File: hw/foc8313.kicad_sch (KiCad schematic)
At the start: 66 parts, among them J1 Tag Connect, J2 CAN, J3 CAN, J4 Aux, P1 USB_C_Plug, SW1 SW_SPST, U1 DRV8313PWP, U10 XC6206P332MR, U2 STM32F103CBTx, U4 AS5047D, U7 LMR36015SFBRNXR, U9 ZD24C08AE1-STGMT, X1 X322516MLB4SI

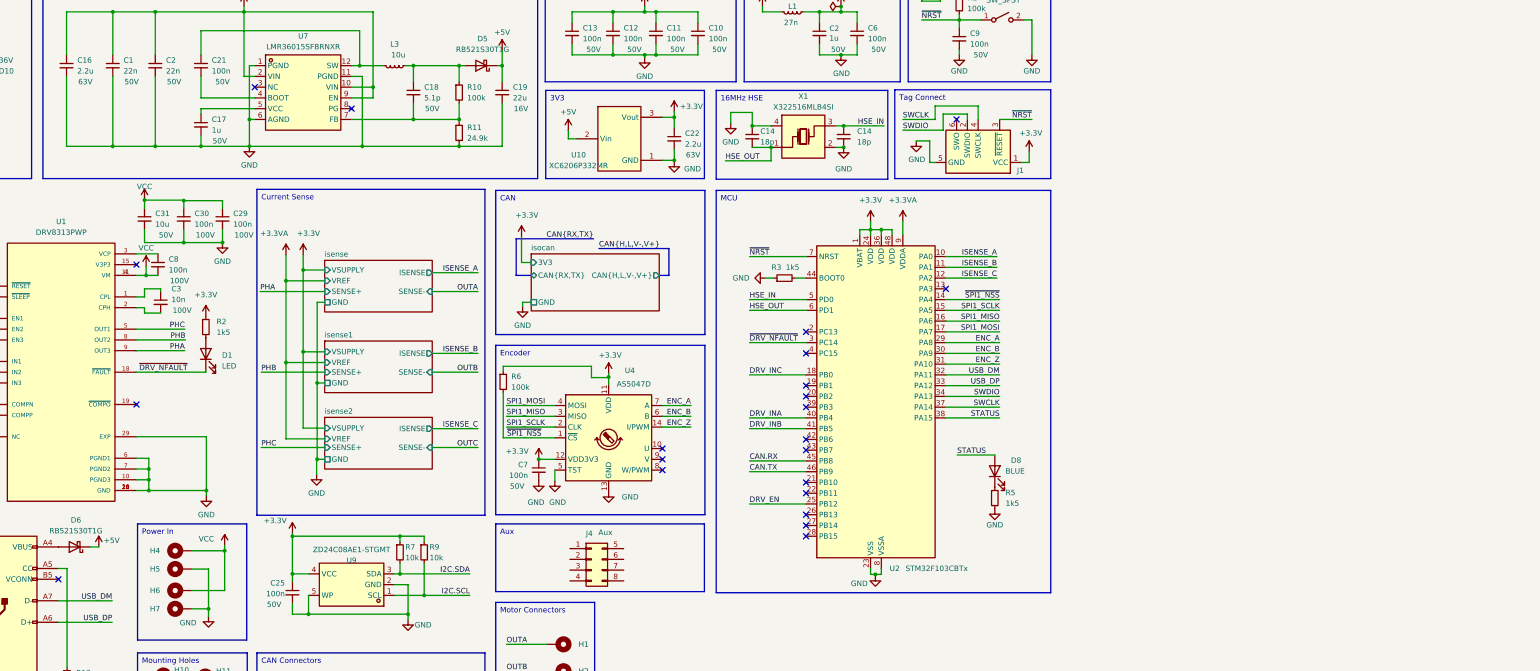
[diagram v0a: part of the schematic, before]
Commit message: [Hw] Cleaning up 5V section
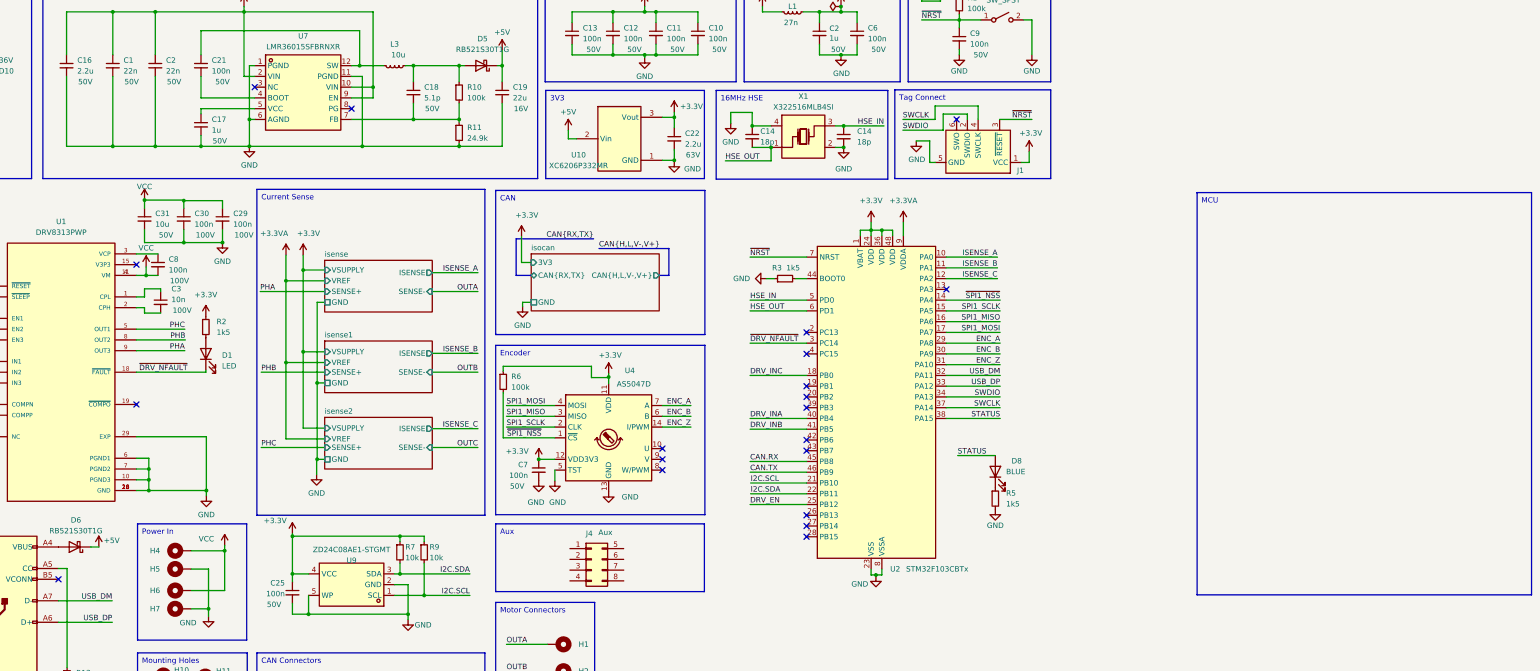
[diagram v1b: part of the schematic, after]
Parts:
- C16: LCSC C6119940 -> C377773; Rating 63V -> 50V
- C18: footprint Capacitor_SMD:C_0603_1608Metric -> Capacitor_SMD:C_0402_1005Metric; LCSC C519110 -> C710655
- C22: LCSC C6119940 -> C377773
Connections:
- net I2C.SCL: now also U2.21 (PB10)
- net I2C.SDA: now also U2.22 (PB11)
- no-connect marks 24 -> 22

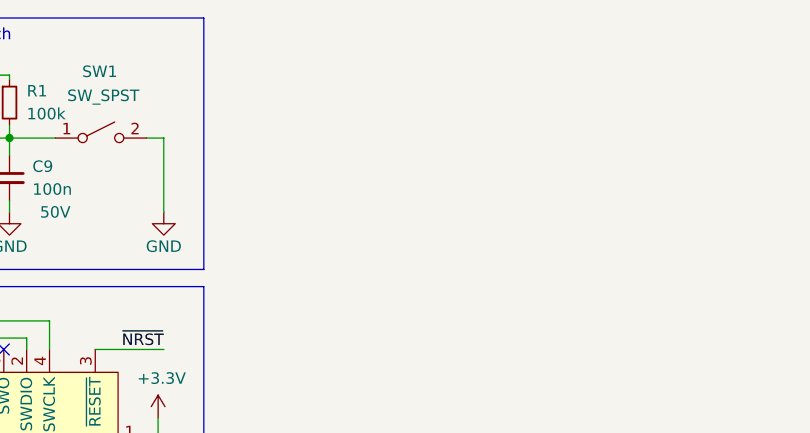
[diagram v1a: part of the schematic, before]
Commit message: [Hw] User button, tag connect placement, eeprom placement
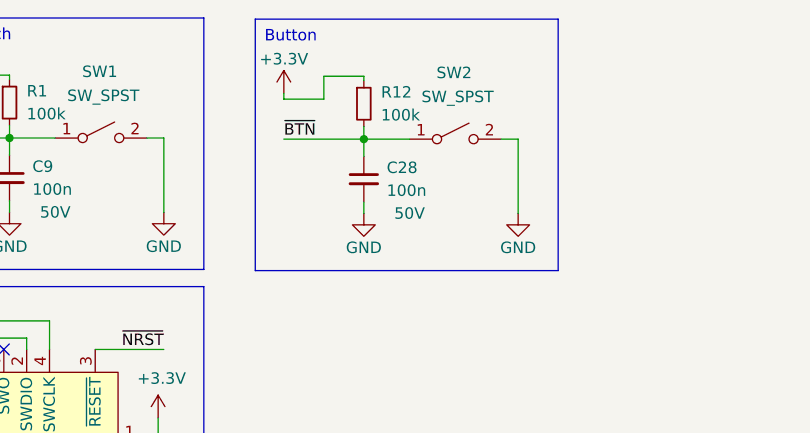
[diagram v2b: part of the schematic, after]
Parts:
- added C28: 100n, Capacitor_SMD:C_0402_1005Metric, symbol Device:C_Small
- added R12: 100k, Resistor_SMD:R_0402_1005Metric, symbol Device:R_Small
- added SW2: SW_SPST, easyeda:SW-SMD_L4.7-W3.5-P3.35-EH, symbol Switch:SW_SPST
- J2, J3: footprint Connector_JST:JST_GH_SM04B-GHS-TB_1x04-1MP_P1.25mm_Horizontal -> easyeda:CONN-SMD_4P-P1.00_INCP_IPCW100W14XXXXR
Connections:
- net +3.3V: now also R12.1
- net GND: now also C28.2, SW2.2 (B)
- new net ~{BTN}: C28.1, R12.2, SW2.1 (A)
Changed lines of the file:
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@@
   (junction (at 86.36 81.153) (diameter 0) (color 0 0 0 0)
   )
+  (junction (at 299.72 28.702) (diameter 0) (color 0 0 0 0)
+  )
   (junction (at 242.062 78.232) (diameter 0) (color 0 0 0 0)
   )
@@
     (stroke (width 0) (type default))
   )
+  (wire (pts (xy 299.72 36.957) (xy 299.72 35.687))
+    (stroke (width 0) (type default))
+  )
   (wire (pts (xy 239.522 78.232) (xy 242.062 78.232))
     (stroke (width 0) (type default))
@@
     (stroke (width 0) (type default))
   )
+  (wire (pts (xy 290.83 24.257) (xy 290.83 23.622))
+    (stroke (width 0) (type default))
+  )
   (wire (pts (xy 153.416 182.372) (xy 163.068 182.372))
     (stroke (width 0) (type default))
@@
     (stroke (width 0) (type default))
   )
+  (wire (pts (xy 290.83 28.702) (xy 299.72 28.702))
+    (stroke (width 0) (type default))
+  )
   (wire (pts (xy 19.05 93.98) (xy 30.48 93.98))
     (stroke (width 0) (type default))
@@
     (stroke (width 0) (type default))
   )
+  (wire (pts (xy 299.72 27.305) (xy 299.72 28.702))
+    (stroke (width 0) (type default))
+  )
   (wire (pts (xy 186.055 26.67) (xy 188.722 26.67))
     (stroke (width 0) (type default))
@@
     (stroke (width 0) (type default))
   )
+  (wire (pts (xy 316.865 36.957) (xy 316.865 28.702))
+    (stroke (width 0) (type default))
+  )
   (wire (pts (xy 78.994 163.322) (xy 86.868 163.322))
     (stroke (width 0) (type default))
@@
     (stroke (width 0) (type default))
   )
+  (wire (pts (xy 299.72 28.702) (xy 304.8 28.702))
+    (stroke (width 0) (type default))
+  )
   (wire (pts (xy 135.89 92.71) (xy 146.685 92.71))
     (stroke (width 0) (type default))
@@
     (stroke (width 0) (type default))
   )
+  (wire (pts (xy 290.83 24.257) (xy 295.275 24.257))
+    (stroke (width 0) (type default))
+  )
   (wire (pts (xy 135.89 107.315) (xy 146.685 107.315))
     (stroke (width 0) (type default))
@@
     (stroke (width 0) (type default))
   )
+  (wire (pts (xy 299.72 28.702) (xy 299.72 30.607))
+    (stroke (width 0) (type default))
+  )
   (wire (pts (xy 68.961 134.62) (xy 68.961 132.08))
     (stroke (width 0) (type default))
@@
     (stroke (width 0) (type default))
   )
+  (wire (pts (xy 295.275 21.717) (xy 299.72 21.717))
+    (stroke (width 0) (type default))
+  )
   (wire (pts (xy 188.722 36.83) (xy 198.628 36.83))
     (stroke (width 0) (type default))
@@
     (stroke (width 0) (type default))
   )
+  (wire (pts (xy 316.865 28.702) (xy 314.96 28.702))
+    (stroke (width 0) (type default))
+  )
   (wire (pts (xy 68.326 86.868) (xy 68.326 88.9))
     (stroke (width 0) (type default))
@@
     (stroke (width 0) (type default))
   )
+  (wire (pts (xy 299.72 21.717) (xy 299.72 22.225))
+    (stroke (width 0) (type default))
+  )
   (wire (pts (xy 178.562 36.83) (xy 186.055 36.83))
     (stroke (width 0) (type default))
@@
     (stroke (width 0) (type default))
   )
+  (wire (pts (xy 295.275 24.257) (xy 295.275 21.717))
+    (stroke (width 0) (type default))
+  )
   (wire (pts (xy 19.05 99.06) (xy 29.21 99.06))
     (stroke (width 0) (type default))
@@
     (effects (font (size 1.27 1.27)) (justify left top))
   )
+  (text_box "Button\n\n"
+    (at 287.655 15.367 0) (size 33.655 27.94)
+    (stroke (width 0) (type default))
+    (fill (type none))
+    (effects (font (size 1.27 1.27)) (justify left top))
+  )
   (text_box "Input: 12V-50V \nOutput: 3.3V@100mA"
     (at 43.942 15.24 0) (size 116.84 50.8)
@@
     (effects (font (size 1.27 1.27)) (justify right bottom))
   )
+  (label "~{BTN}" (at 290.83 28.702 0) (fields_autoplaced)
+    (effects (font (size 1.27 1.27)) (justify left bottom))
+  )
   (label "SPI1_MOSI" (at 270.002 102.362 180) (fields_autoplaced)
     (effects (font (size 1.27 1.27)) (justify right bottom))
@@
     )
   )
+  (symbol (lib_id "Device:R_Small") (at 299.72 24.765 0) (unit 1)
+    (in_bom yes) (on_board yes) (dnp no)
+    (property "Reference" "R12" (at 301.625 23.495 0)
+      (effects (font (size 1.27 1.27)) (justify left))
+    )
+    (property "Value" "100k" (at 301.625 26.035 0)
+      (effects (font (size 1.27 1.27)) (justify left))
+    )
+    (property "Footprint" "Resistor_SMD:R_0402_1005Metric" (at 299.72 24.765 0)
+      (effects (font (size 1.27 1.27)) hide)
+    )
+    (property "Datasheet" "~" (at 299.72 24.765 0)
+      (effects (font (size 1.27 1.27)) hide)
+    )
+    (property "LCSC" "C25741" (at 299.72 24.765 0)
+      (effects (font (size 1.27 1.27)) hide)
+    )
+    (pin "1")
+    (pin "2")
+    (instances
+      (project "foc8313"
+        (path "/6a0f293a-1ae1-497a-a3c1-0d8f9e6f81b9"
+          (reference "R12") (unit 1)
+        )
+      )
+    )
+  )
   (symbol (lib_id "Connector_Generic:Conn_02x04_Top_Bottom") (at 173.482 155.956 0) (unit 1)
     (in_bom yes) (on_board yes) (dnp no)
@@
     )
   )
+  (symbol (lib_id "power:GND") (at 299.72 36.957 0) (unit 1)
+    (in_bom yes) (on_board yes) (dnp no)
+    (property "Reference" "#PWR048" (at 299.72 43.307 0)
+      (effects (font (size 1.27 1.27)) hide)
+    )
+    (property "Value" "GND" (at 299.72 40.767 0)
+      (effects (font (size 1.27 1.27)))
+    )
+    (property "Footprint" "" (at 299.72 36.957 0)
+      (effects (font (size 1.27 1.27)) hide)
+    )
+    (property "Datasheet" "" (at 299.72 36.957 0)
+      (effects (font (size 1.27 1.27)) hide)
+    )
+    (pin "1")
+    (instances
+      (project "foc8313"
+        (path "/6a0f293a-1ae1-497a-a3c1-0d8f9e6f81b9"
+          (reference "#PWR048") (unit 1)
+        )
+      )
+    )
+  )
   (symbol (lib_id "Switch:SW_SPST") (at 270.51 28.575 0) (unit 1)
     (in_bom yes) (on_board yes) (dnp no)
@@
       (effects (font (size 1.27 1.27)) (justify right))
     )
-    (property "Footprint" "Connector_JST:JST_GH_SM04B-GHS-TB_1x04-1MP_P1.25mm_Horizontal" (at 100.838 190.246 0)
+    (property "Footprint" "easyeda:CONN-SMD_4P-P1.00_INCP_IPCW100W14XXXXR" (at 100.838 190.246 0)
       (effects (font (size 1.27 1.27)) hide)
     )
@@
     )
   )
+  (symbol (lib_id "power:GND") (at 316.865 36.957 0) (unit 1)
+    (in_bom yes) (on_board yes) (dnp no)
+    (property "Reference" "#PWR049" (at 316.865 43.307 0)
+      (effects (font (size 1.27 1.27)) hide)
+    )
+    (property "Value" "GND" (at 316.865 40.767 0)
+      (effects (font (size 1.27 1.27)))
+    )
+    (property "Footprint" "" (at 316.865 36.957 0)
+      (effects (font (size 1.27 1.27)) hide)
+    )
+    (property "Datasheet" "" (at 316.865 36.957 0)
+      (effects (font (size 1.27 1.27)) hide)
+    )
+    (pin "1")
+    (instances
+      (project "foc8313"
+        (path "/6a0f293a-1ae1-497a-a3c1-0d8f9e6f81b9"
+          (reference "#PWR049") (unit 1)
+        )
+      )
+    )
+  )
   (symbol (lib_id "Device:R_Small") (at 82.423 101.092 0) (unit 1)
     (in_bom yes) (on_board yes) (dnp no) (fields_autoplaced)
@@
     )
   )
+  (symbol (lib_name "+3.3V_2") (lib_id "power:+3.3V") (at 290.83 23.622 0) (unit 1)
+    (in_bom yes) (on_board yes) (dnp no)
+    (property "Reference" "#PWR029" (at 290.83 27.432 0)
+      (effects (font (size 1.27 1.27)) hide)
+    )
+    (property "Value" "+3.3V" (at 290.83 19.812 0)
+      (effects (font (size 1.27 1.27)))
+    )
+    (property "Footprint" "" (at 290.83 23.622 0)
+      (effects (font (size 1.27 1.27)) hide)
+    )
+    (property "Datasheet" "" (at 290.83 23.622 0)
+      (effects (font (size 1.27 1.27)) hide)
+    )
+    (pin "1")
+    (instances
+      (project "foc8313"
+        (path "/6a0f293a-1ae1-497a-a3c1-0d8f9e6f81b9"
+          (reference "#PWR029") (unit 1)
+        )
+      )
+    )
+  )
   (symbol (lib_id "power:GND") (at 157.226 96.266 0) (unit 1)
     (in_bom yes) (on_board yes) (dnp no) (fields_autoplaced)
@@
       (effects (font (size 1.27 1.27)) (justify right))
     )
-    (property "Footprint" "Connector_JST:JST_GH_SM04B-GHS-TB_1x04-1MP_P1.25mm_Horizontal" (at 135.89 190.246 0)
+    (property "Footprint" "easyeda:CONN-SMD_4P-P1.00_INCP_IPCW100W14XXXXR" (at 135.89 190.246 0)
       (effects (font (size 1.27 1.27)) hide)
     )
@@
     )
   )
+  (symbol (lib_id "Device:C_Small") (at 299.72 33.147 0) (unit 1)
+    (in_bom yes) (on_board yes) (dnp no)
+    (property "Reference" "C28" (at 302.26 31.877 0)
+      (effects (font (size 1.27 1.27)) (justify left))
+    )
+    (property "Value" "100n" (at 302.26 34.417 0)
+      (effects (font (size 1.27 1.27)) (justify left))
+    )
+    (property "Footprint" "Capacitor_SMD:C_0402_1005Metric" (at 299.72 33.147 0)
+      (effects (font (size 1.27 1.27)) hide)
+    )
+    (property "Datasheet" "~" (at 299.72 33.147 0)
+      (effects (font (size 1.27 1.27)) hide)
+    )
+    (property "Rating" "50V" (at 304.8 36.957 0)
+      (effects (font (size 1.27 1.27)))
+    )
+    (property "LCSC" "C307331" (at 299.72 33.147 0)
+      (effects (font (size 1.27 1.27)) hide)
+    )
+    (pin "1")
+    (pin "2")
+    (instances
+      (project "foc8313"
+        (path "/6a0f293a-1ae1-497a-a3c1-0d8f9e6f81b9"
+          (reference "C28") (unit 1)
+        )
+      )
+    )
+  )
   (symbol (lib_id "Device:L_Small") (at 127 39.37 270) (unit 1)
     (in_bom yes) (on_board yes) (dnp no)
@@
         )
       )
+    )
+  )
+  (symbol (lib_id "Switch:SW_SPST") (at 309.88 28.702 0) (unit 1)
+    (in_bom yes) (on_board yes) (dnp no)
+    (property "Reference" "SW2" (at 309.753 21.336 0)
+      (effects (font (size 1.27 1.27)))
+    )
+    (property "Value" "SW_SPST" (at 310.134 24.003 0)
+      (effects (font (size 1.27 1.27)))
+    )
+    (property "Footprint" "easyeda:SW-SMD_L4.7-W3.5-P3.35-EH" (at 309.88 28.702 0)
+      (effects (font (size 1.27 1.27)) hide)
+    )
+    (property "Datasheet" "~" (at 309.88 28.702 0)
+      (effects (font (size 1.27 1.27)) hide)
+    )
+    (pin "1")
+    (pin "2")
+    (instances
+      (project "foc8313"
+        (path "/6a0f293a-1ae1-497a-a3c1-0d8f9e6f81b9"
+          (reference "SW2") (unit 1)
+        )
+      )

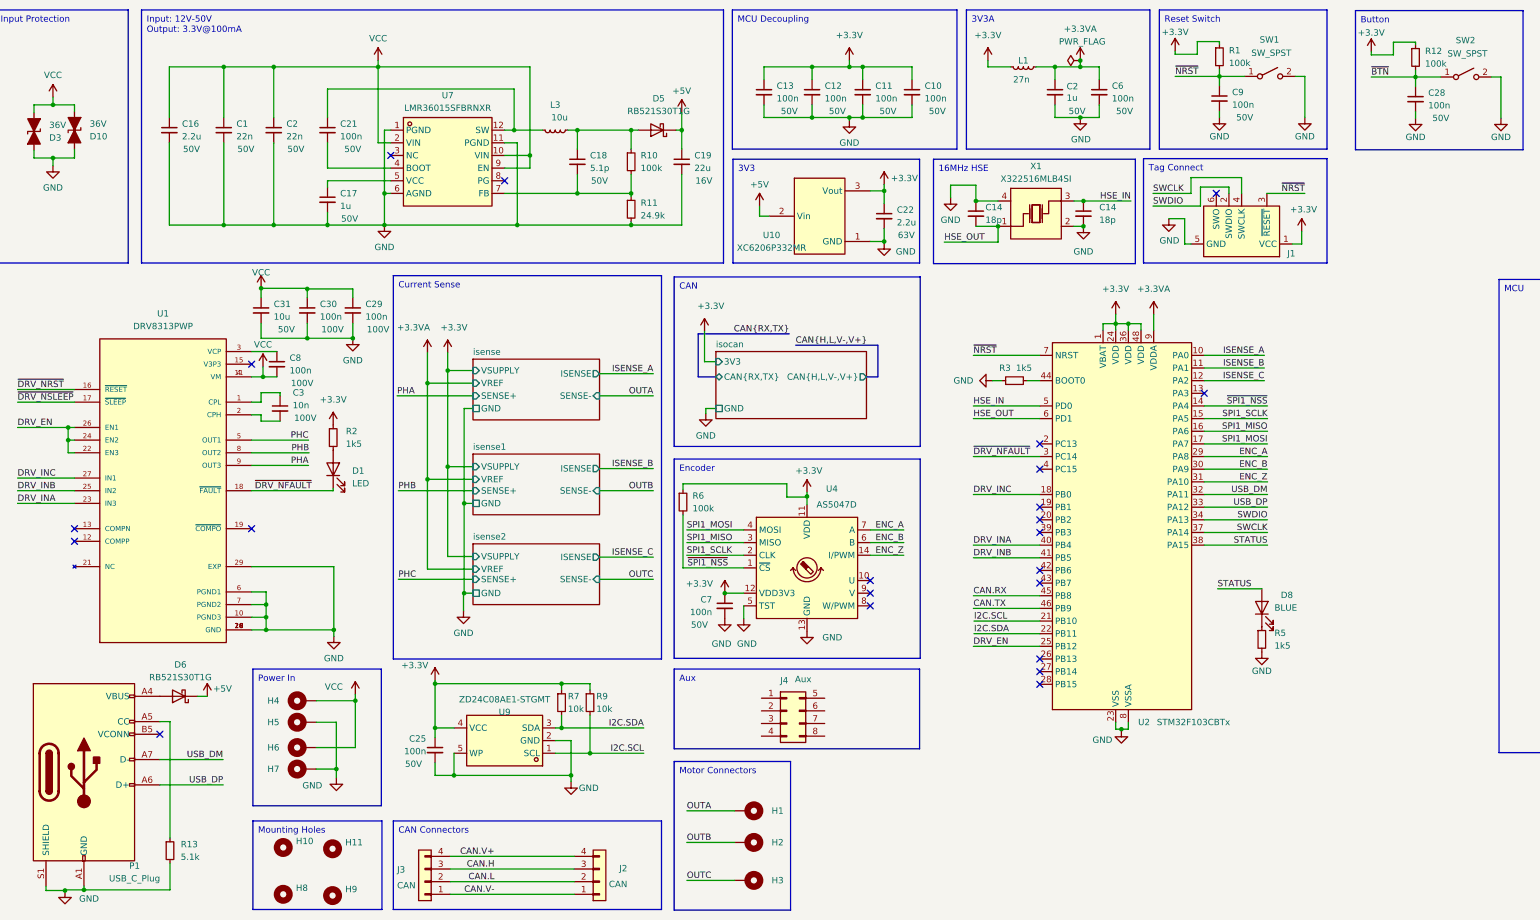
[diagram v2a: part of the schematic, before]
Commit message: [Hw] Small ICs to make 3 wire can possible in this formfactor
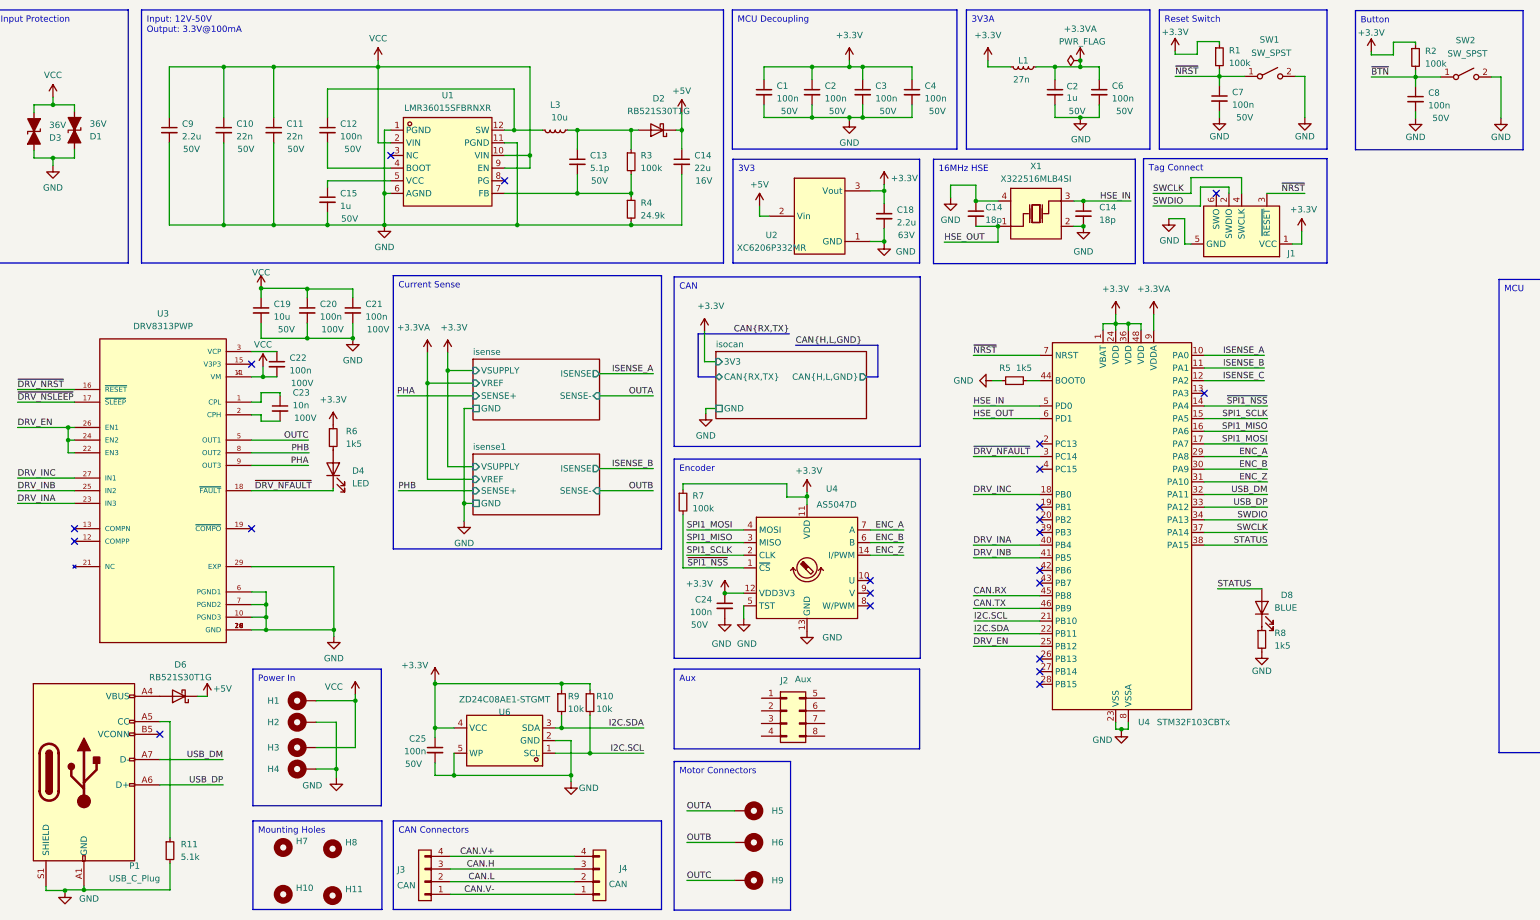
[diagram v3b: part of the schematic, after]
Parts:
- renumbered C13 to C1, C1 to C10, C2 to C11, C21 to C12, C18 to C13, C19 to C14, C17 to C15, C22 to C18, C31 to C19, C12 to C2, C30 to C20, C29 to C21, C8 to C22, C3 to C23, C7 to C24, C11 to C3, C10 to C4, C9 to C7, C28 to C8, C16 to C9, D10 to D1, D5 to D2, D1 to D4, H4 to H1, H8 to H10, H9 to H11, H5 to H2, H6 to H3, H7 to H4, H1 to H5, H2 to H6, H10 to H7, H11 to H8, H3 to H9, J4 to J2, J2 to J4, R9 to R10, R13 to R11, R12 to R2, R10 to R3, R11 to R4, R3 to R5, R2 to R6, R6 to R7, R5 to R8, R7 to R9, U7 to U1, U10 to U2, U1 to U3, U2 to U4, U9 to U6
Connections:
- net PHC is gone; now on net OUTC: U3.5 (OUT1)
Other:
- removed sheet isense2
- sheet isocan ports: added CAN{H,L,GND}; removed CAN{H,L,V-,V+}
